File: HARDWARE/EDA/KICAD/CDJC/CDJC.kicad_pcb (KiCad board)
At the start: 2 copper layers, 64 parts, among them J1 COM_IN, J2 COM_OUT, J3 POWER_IN, J4 POWER_OUT, J5 BIT_OUT, Q1 BC549, SW1 B-SET, U1 74LS04, U2 74LS32, U3 74LS08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

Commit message: i am crazy
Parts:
- removed C1: 1800µF 6.3V, Capacitor_THT:CP_Radial_D10.0mm_P5.00mm
- J2, J4, J5: moved to B.Cu
- moved J3 161.1 mm to (182.7, 45.0), turned to 0 degrees
- moved J1 149.6 mm to (182.7, 52.3), turned to 0 degrees
- moved SW1 129.4 mm to (175.0, 51.0), turned to 180 degrees
- moved U1 120.7 mm to (149.5, 81.8), turned to 180 degrees
- moved U4 118.4 mm to (134.0, 135.2), turned to 180 degrees
- moved R6 115.8 mm to (163.4, 53.5)
- moved D3 111.8 mm to (161.1, 45.0), turned to 0 degrees
- moved R3 111.8 mm to (161.2, 53.5)
- moved R5 107.3 mm to (158.2, 53.5)
- moved R2 103.5 mm to (156.0, 53.5)
- moved D2 101.6 mm to (155.9, 45.0), turned to 0 degrees
- moved R4 99.5 mm to (153.1, 53.5)
- moved R1 96.1 mm to (151.0, 53.5)
- moved J4 95.4 mm to (184.2, 117.9)
- moved D1 93.8 mm to (150.7, 45.0), turned to 0 degrees
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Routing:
- net GNDD: track 19.0 -> 87.2 mm
- net LB_SW: track 0.00 -> 20.3 mm
- net +5VD: track 20.0 -> 34.2 mm
- net NB_SW: track 0.00 -> 12.0 mm
- net Net-(U5-Pad10): track 29.2 -> 18.8 mm
- net LBMon: track 10.8 -> 1.04 mm
- net Net-(U8-Pad11): track 0.00 -> 7.62 mm
- net FB_SW: track 0.00 -> 5.01 mm
- net Net-(D1-Pad2): track 0.00 -> 3.50 mm
- net Net-(D2-Pad2): track 0.00 -> 3.48 mm
- net Net-(D3-Pad2): track 0.00 -> 3.48 mm
- net Net-(D5-Pad2): track 0.00 -> 3.45 mm
- net Net-(D7-Pad2): track 0.00 -> 3.43 mm
- net Net-(D8-Pad2): track 0.00 -> 3.42 mm
- net Net-(D6-Pad2): track 0.00 -> 3.40 mm
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
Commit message: i am crazy
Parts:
- D10, D11, D13, D14, D15, D16, D17, D18, D19, D20, D21, D9: footprint Diode_THT:D_DO-34_SOD68_P2.54mm_Vertical_AnodeUp -> Diode_THT:D_DO-34_SOD68_P7.62mm_Horizontal
- J1: footprint Connector_PinHeader_2.00mm:PinHeader_1x05_P2.00mm_Horizontal -> Connector_PinHeader_2.54mm:PinHeader_1x05_P2.54mm_Horizontal
- J2: footprint Connector_PinSocket_2.00mm:PinSocket_1x05_P2.00mm_Horizontal -> Connector_PinSocket_2.54mm:PinSocket_1x05_P2.54mm_Horizontal
- J3: footprint Connector_PinHeader_2.00mm:PinHeader_1x03_P2.00mm_Horizontal -> Connector_PinHeader_2.54mm:PinHeader_1x03_P2.54mm_Horizontal
- J4: footprint Connector_PinSocket_2.00mm:PinSocket_1x03_P2.00mm_Horizontal -> Connector_PinSocket_2.54mm:PinSocket_1x03_P2.54mm_Horizontal
- J5: footprint Connector_PinSocket_2.00mm:PinSocket_1x08_P2.00mm_Horizontal -> Connector_PinSocket_2.54mm:PinSocket_1x08_P2.54mm_Horizontal
- R1, R10, R11, R12, R13, R14, R15, R16, R17, R2, R3, R4, R5, R6, R7, R8, R9: footprint Resistor_THT:R_Axial_DIN0204_L3.6mm_D1.6mm_P5.08mm_Horizontal -> Resistor_THT:R_Axial_DIN0207_L6.3mm_D2.5mm_P7.62mm_Horizontal
- moved SW1 83.1 mm to (92.0, 46.8), turned to 0 degrees
- moved D20 60.9 mm to (95.5, 106.8)
- moved D9 55.8 mm to (100.6, 114.6)
- moved U5 55.8 mm to (113.5, 122.1)
- moved C5 55.8 mm to (105.9, 125.3)
- moved D12 55.8 mm to (118.4, 122.6)
- moved D21 55.8 mm to (103.2, 109.3)
- moved Q1 55.8 mm to (120.2, 112.1)
- moved R15 55.8 mm to (116.2, 106.8)
- moved R16 55.8 mm to (121.2, 117.3)
- moved R17 55.8 mm to (116.2, 117.7)
- moved C8 54.1 mm to (176.8, 95.6), turned to 90 degrees
- moved U4 52.5 mm to (113.2, 87.0), turned to 270 degrees
- moved U7 51.8 mm to (173.6, 88.0), turned to 270 degrees
- moved C3 49.3 mm to (176.8, 76.3), turned to 90 degrees
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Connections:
- U2 pad 1: LB_SW -> GNDD
- U2 pad 10: NB_SW -> LB_SW
- U2 pad 11: Net-(U2-Pad11) -> Net-(U1-Pad9)
- U2 pad 12: GNDD -> FB_SW
- U2 pad 13: GNDD -> NB_SW
- U2 pad 2: NB_SW -> GNDD
- U2 pad 3: Net-(U1-Pad9) -> Net-(U2-Pad3)
- U2 pad 4: FB_SW -> NB_SW
- U2 pad 6: Net-(U1-Pad11) -> Net-(U1-Pad13)
- U2 pad 8: Net-(U1-Pad13) -> Net-(U1-Pad11)
- U3 pad 1: Net-(U1-Pad8) -> Net-(U1-Pad12)
- U3 pad 9: Net-(U1-Pad12) -> Net-(U1-Pad8)
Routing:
- net FB_SW: track 5.01 -> 68.2 mm
- net Net-(U1-Pad13): track 0.00 -> 44.6 mm
- net Net-(U1-Pad11): track 0.00 -> 42.8 mm
- net NB_SW: track 12.0 -> 40.2 mm
- net Net-(U1-Pad9): track 0.00 -> 26.6 mm
- net LB_SW: track 20.3 -> 30.1 mm
- net GNDD: track 87.2 -> 79.6 mm
- net Net-(D5-Pad2): track 3.45 -> 0.00 mm
- net Net-(D7-Pad2): track 3.43 -> 0.00 mm
- net Net-(D8-Pad2): track 3.42 -> 0.00 mm
- net Net-(D6-Pad2): track 3.40 -> 0.00 mm
- net Net-(D4-Pad2): track 3.37 -> 0.00 mm
- net MRI: track 2.50 -> 0.00 mm
- net LBLBI: track 2.50 -> 0.00 mm
- net EI: track 2.50 -> 0.00 mm
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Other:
- board outline added: 116.7 x 101.5 mm

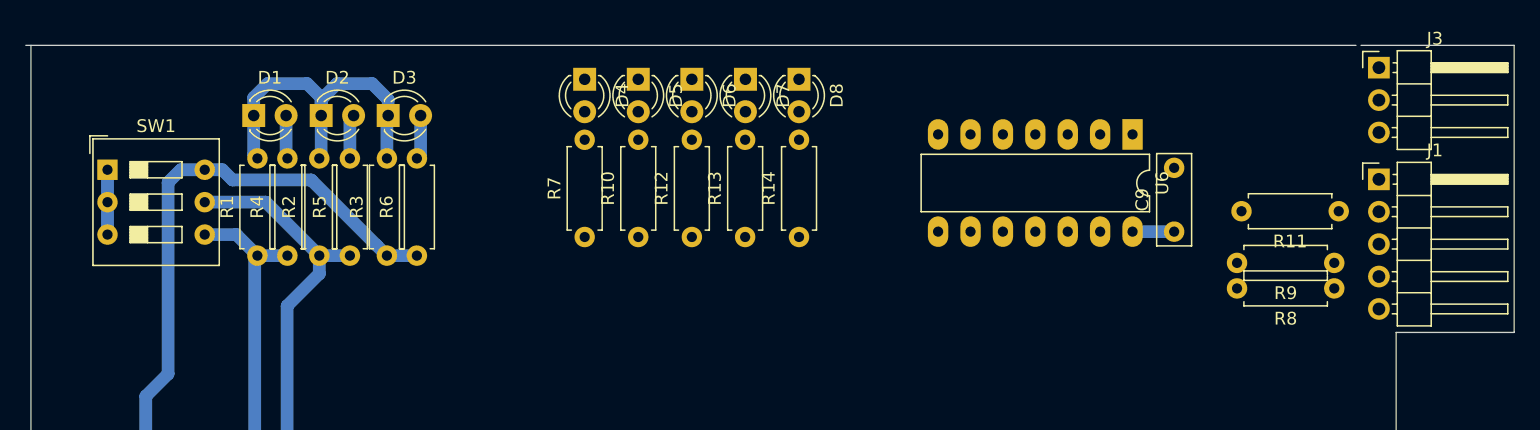
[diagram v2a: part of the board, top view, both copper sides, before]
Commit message: PCI connector OK
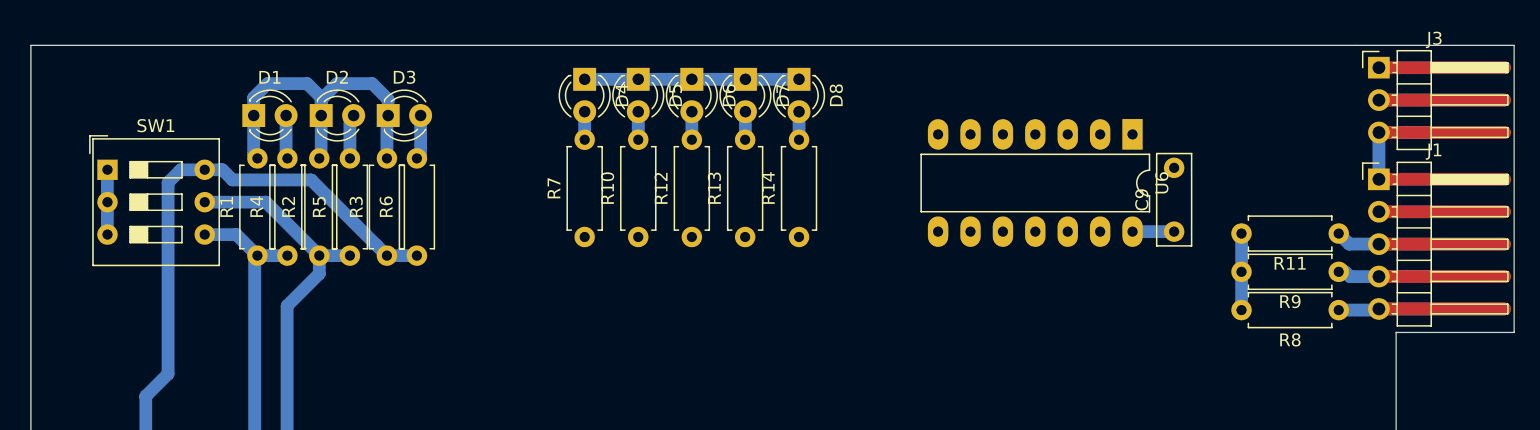
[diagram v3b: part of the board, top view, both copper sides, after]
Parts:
- moved R11 1.75 mm to (188.5, 51.8)
- moved R8 1.74 mm to (188.5, 57.8)
- moved R9 0.78 mm to (188.5, 54.8)
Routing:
- net GNDD: track 79.6 -> 165.2 mm
- net LBLBI: track 0.00 -> 23.2 mm
- net MRI: track 0.00 -> 23.0 mm
- net EI: track 0.00 -> 22.9 mm
- net CLK: track 0.00 -> 19.7 mm
- net +5VD: track 34.7 -> 54.4 mm
- net Net-(D7-Pad2): track 0.00 -> 2.21 mm
- net Net-(D8-Pad2): track 0.00 -> 2.20 mm
- net Net-(D6-Pad2): track 0.00 -> 2.20 mm
- net Net-(D5-Pad2): track 0.00 -> 2.20 mm
- net Net-(D4-Pad2): track 0.00 -> 2.20 mm
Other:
- board size 116.7 x 101.5 mm -> 116.2 x 101.5 mm
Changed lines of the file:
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@@
   (general
     (thickness 1.6)
-    (drawings 7)
-    (tracks 174)
+    (drawings 9)
+    (tracks 206)
     (zones 0)
     (modules 63)
@@
   )
   (module Resistor_THT:R_Axial_DIN0207_L6.3mm_D2.5mm_P7.62mm_Horizontal (layer F.Cu)
-    (at 188.5 50 180)
+    (at 188.5 51.75 180)
     (descr "Resistor, Axial_DIN0207 series, Axial, Horizontal, pin pitch=7.62mm, 0.25W = 1/4W, length*diameter=6.3*2.5mm^2, http://cdn-reichelt.de/documents/datenblatt/B400/1_4W%23YAG.pdf")
     (tags "Resistor Axial_DIN0207 series Axial Horizontal pin pitch 7.62mm 0.25W = 1/4W length 6.3mm diameter 2.5mm")
@@
   )
   (module Resistor_THT:R_Axial_DIN0207_L6.3mm_D2.5mm_P7.62mm_Horizontal (layer F.Cu)
-    (at 188.15 54.05 180)
+    (at 188.5 54.75 180)
     (descr "Resistor, Axial_DIN0207 series, Axial, Horizontal, pin pitch=7.62mm, 0.25W = 1/4W, length*diameter=6.3*2.5mm^2, http://cdn-reichelt.de/documents/datenblatt/B400/1_4W%23YAG.pdf")
     (tags "Resistor Axial_DIN0207 series Axial Horizontal pin pitch 7.62mm 0.25W = 1/4W length 6.3mm diameter 2.5mm")
@@
   )
   (module Resistor_THT:R_Axial_DIN0207_L6.3mm_D2.5mm_P7.62mm_Horizontal (layer F.Cu)
-    (at 188.15 56.05 180)
+    (at 188.5 57.75 180)
     (descr "Resistor, Axial_DIN0207 series, Axial, Horizontal, pin pitch=7.62mm, 0.25W = 1/4W, length*diameter=6.3*2.5mm^2, http://cdn-reichelt.de/documents/datenblatt/B400/1_4W%23YAG.pdf")
     (tags "Resistor Axial_DIN0207 series Axial Horizontal pin pitch 7.62mm 0.25W = 1/4W length 6.3mm diameter 2.5mm")
@@
     )
   )
-  (gr_line (start 85.6 37) (end 189.85 37) (layer Edge.Cuts) (width 0.05))
+  (gr_poly (pts (xy 202.1 59.4) (xy 193 59.4) (xy 193 37.1) (xy 202.1 37.1)) (layer B.Mask) (width 0.1))
+  (gr_poly (pts (xy 202.1 59.4) (xy 193 59.4) (xy 193 37.1) (xy 202.1 37.1)) (layer F.Mask) (width 0.1))
+  (gr_line (start 86 37) (end 189.85 37) (layer Edge.Cuts) (width 0.05))
   (gr_line (start 86 138.5) (end 86 37) (layer Edge.Cuts) (width 0.05))
   (gr_line (start 193 138.5) (end 86 138.5) (layer Edge.Cuts) (width 0.05))
@@
   (gr_line (start 202.25 59.5) (end 193 59.5) (layer Edge.Cuts) (width 0.05))
   (gr_line (start 202.25 37) (end 202.25 59.5) (layer Edge.Cuts) (width 0.05))
-  (gr_line (start 190.25 37) (end 202.25 37) (layer Edge.Cuts) (width 0.05))
+  (gr_line (start 189.85 37) (end 202.25 37) (layer Edge.Cuts) (width 0.05))
+  (segment (start 191.65 50.04) (end 201.5 50.04) (width 1) (layer F.Cu) (net 38))
+  (segment (start 191.65 41.29) (end 201.5 41.29) (width 1) (layer F.Cu) (net 2))
+  (segment (start 191.65 52.58) (end 201.5 52.58) (width 1) (layer F.Cu) (net 37))
+  (segment (start 191.65 57.66) (end 201.5 57.66) (width 1) (layer F.Cu) (net 35))
+  (segment (start 191.65 43.83) (end 201.5 43.83) (width 1) (layer F.Cu) (net 1))
+  (segment (start 191.65 47.5) (end 201.5 47.5) (width 1) (layer F.Cu) (net 1))
+  (segment (start 191.65 38.75) (end 201.5 38.75) (width 1) (layer F.Cu) (net 1))
+  (segment (start 191.65 55.12) (end 201.5 55.12) (width 1) (layer F.Cu) (net 36))
   (segment (start 116.14 106.86) (end 116.15 106.85) (width 1) (layer B.Cu) (net 1))
   (segment (start 113.52 106.86) (end 116.14 106.86) (width 1) (layer B.Cu) (net 1))
@@
   (segment (start 113.7 68.7) (end 115.2 68.7) (width 1) (layer B.Cu) (net 1))
   (segment (start 111.16 68.7) (end 113.7 68.7) (width 1) (layer B.Cu) (net 1))
+  (segment (start 129.4 39.66) (end 146.2 39.66) (width 1) (layer B.Cu) (net 1))
+  (segment (start 180.88 57.75) (end 180.88 51.75) (width 1) (layer B.Cu) (net 1))
+  (segment (start 191.65 43.83) (end 191.65 47.5) (width 1) (layer B.Cu) (net 1))
+  (segment (start 191.65 47.5) (end 201.5 47.5) (width 1) (layer B.Cu) (net 1))
+  (segment (start 191.65 43.83) (end 201.5 43.83) (width 1) (layer B.Cu) (net 1))
+  (segment (start 191.65 38.75) (end 201.5 38.75) (width 1) (layer B.Cu) (net 1))
   (segment (start 116.18 76.32) (end 117 75.5) (width 1) (layer B.Cu) (net 2))
   (segment (start 113.7 76.32) (end 116.18 76.32) (width 1) (layer B.Cu) (net 2))
+  (segment (start 191.65 41.29) (end 201.5 41.29) (width 1) (layer B.Cu) (net 2))
+  (segment (start 129.4 42.2) (end 129.4 44.4) (width 1) (layer B.Cu) (net 6))
+  (segment (start 133.6 42.2) (end 133.6 44.4) (width 1) (layer B.Cu) (net 7))
+  (segment (start 137.8 42.2) (end 137.8 44.4) (width 1) (layer B.Cu) (net 8))
+  (segment (start 142 44.376969) (end 141.976969 44.4) (width 1) (layer B.Cu) (net 9))
+  (segment (start 142 42.2) (end 142 44.376969) (width 1) (layer B.Cu) (net 9))
+  (segment (start 146.2 42.2) (end 146.2 44.4) (width 1) (layer B.Cu) (net 10))
+  (segment (start 191.56 57.75) (end 191.65 57.66) (width 1) (layer B.Cu) (net 35))
+  (segment (start 188.5 57.75) (end 191.56 57.75) (width 1) (layer B.Cu) (net 35))
+  (segment (start 191.65 57.66) (end 201.5 57.66) (width 1) (layer B.Cu) (net 35))
+  (segment (start 188.5 54.75) (end 189 54.75) (width 1) (layer B.Cu) (net 36))
+  (segment (start 189.37 55.12) (end 191.65 55.12) (width 1) (layer B.Cu) (net 36))
+  (segment (start 189 54.75) (end 189.37 55.12) (width 1) (layer B.Cu) (net 36))
+  (segment (start 191.65 55.12) (end 201.5 55.12) (width 1) (layer B.Cu) (net 36))
+  (segment (start 189.33 52.58) (end 191.65 52.58) (width 1) (layer B.Cu) (net 37))
+  (segment (start 188.5 51.75) (end 189.33 52.58) (width 1) (layer B.Cu) (net 37))
+  (segment (start 191.65 52.58) (end 201.5 52.58) (width 1) (layer B.Cu) (net 37))
+  (segment (start 191.65 50.04) (end 201.5 50.04) (width 1) (layer B.Cu) (net 38))
   (segment (start 111.16 74.12) (end 109.04 72) (width 1) (layer B.Cu) (net 42))
   (segment (start 111.16 76.32) (end 111.16 74.12) (width 1) (layer B.Cu) (net 42))

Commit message: stop work
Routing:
- net LBLBI: track 23.2 -> 87.5 mm
- net MRI: track 23.0 -> 62.2 mm
- net FBMon: track 0.00 -> 37.5 mm
- net MRLMon: track 0.00 -> 29.2 mm, vias 0 -> 1
- net EI: track 22.9 -> 50.0 mm
- net Net-(U6-Pad11): track 0.00 -> 17.7 mm
- net LBMon: track 1.04 -> 17.3 mm
- net Net-(U6-Pad2): track 0.00 -> 9.46 mm
- net LB_SW: track 30.1 -> 34.4 mm, vias 0 -> 1
- net GNDD: track 165.2 -> 168.5 mm
- net Net-(U1-Pad11): track 42.8 -> 44.2 mm
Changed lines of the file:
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@@
     (thickness 1.6)
     (drawings 9)
-    (tracks 206)
+    (tracks 261)
     (zones 0)
     (modules 63)
@@
   (segment (start 191.65 43.83) (end 201.5 43.83) (width 1) (layer B.Cu) (net 1))
   (segment (start 191.65 38.75) (end 201.5 38.75) (width 1) (layer B.Cu) (net 1))
+  (segment (start 96.66 68.7) (end 95.6 69.76) (width 1) (layer F.Cu) (net 1))
+  (segment (start 98.46 68.7) (end 96.66 68.7) (width 1) (layer F.Cu) (net 1))
   (segment (start 116.18 76.32) (end 117 75.5) (width 1) (layer B.Cu) (net 2))
   (segment (start 113.7 76.32) (end 116.18 76.32) (width 1) (layer B.Cu) (net 2))
@@
   (segment (start 188.5 57.75) (end 191.56 57.75) (width 1) (layer B.Cu) (net 35))
   (segment (start 191.65 57.66) (end 201.5 57.66) (width 1) (layer B.Cu) (net 35))
+  (segment (start 179.18 43.98) (end 172.34 43.98) (width 1) (layer B.Cu) (net 35))
+  (segment (start 182.6 47.4) (end 179.18 43.98) (width 1) (layer B.Cu) (net 35))
+  (segment (start 182.6 56.4) (end 182.6 47.4) (width 1) (layer B.Cu) (net 35))
+  (segment (start 183.95 57.75) (end 182.6 56.4) (width 1) (layer B.Cu) (net 35))
+  (segment (start 188.5 57.75) (end 183.95 57.75) (width 1) (layer B.Cu) (net 35))
   (segment (start 188.5 54.75) (end 189 54.75) (width 1) (layer B.Cu) (net 36))
   (segment (start 189.37 55.12) (end 191.65 55.12) (width 1) (layer B.Cu) (net 36))
   (segment (start 189 54.75) (end 189.37 55.12) (width 1) (layer B.Cu) (net 36))
   (segment (start 191.65 55.12) (end 201.5 55.12) (width 1) (layer B.Cu) (net 36))
+  (segment (start 188.5 54.75) (end 185.35 54.75) (width 1) (layer B.Cu) (net 36))
+  (segment (start 185.35 54.75) (end 184.3 53.7) (width 1) (layer B.Cu) (net 36))
+  (segment (start 184.3 53.7) (end 184.3 45.4) (width 1) (layer B.Cu) (net 36))
+  (segment (start 184.3 45.4) (end 180.1 41.2) (width 1) (layer B.Cu) (net 36))
+  (segment (start 162.18 41.78) (end 162.18 43.98) (width 1) (layer B.Cu) (net 36))
+  (segment (start 162.76 41.2) (end 162.18 41.78) (width 1) (layer B.Cu) (net 36))
+  (segment (start 180.1 41.2) (end 162.76 41.2) (width 1) (layer B.Cu) (net 36))
   (segment (start 189.33 52.58) (end 191.65 52.58) (width 1) (layer B.Cu) (net 37))
   (segment (start 188.5 51.75) (end 189.33 52.58) (width 1) (layer B.Cu) (net 37))
   (segment (start 191.65 52.58) (end 201.5 52.58) (width 1) (layer B.Cu) (net 37))
+  (segment (start 159.64 53.8) (end 159.64 51.6) (width 1) (layer B.Cu) (net 37))
+  (segment (start 159.04 54.4) (end 159.64 53.8) (width 1) (layer B.Cu) (net 37))
+  (segment (start 153.8 51.6) (end 156.6 54.4) (width 1) (layer B.Cu) (net 37))
+  (segment (start 181.3 39.1) (end 156.3 39.1) (width 1) (layer B.Cu) (net 37))
+  (segment (start 153.8 41.6) (end 153.8 51.6) (width 1) (layer B.Cu) (net 37))
+  (segment (start 156.3 39.1) (end 153.8 41.6) (width 1) (layer B.Cu) (net 37))
+  (segment (start 186.4 44.2) (end 181.3 39.1) (width 1) (layer B.Cu) (net 37))
+  (segment (start 156.6 54.4) (end 159.04 54.4) (width 1) (layer B.Cu) (net 37))
+  (segment (start 186.4 50.78137) (end 186.4 44.2) (width 1) (layer B.Cu) (net 37))
+  (segment (start 187.36863 51.75) (end 186.4 50.78137) (width 1) (layer B.Cu) (net 37))
+  (segment (start 188.5 51.75) (end 187.36863 51.75) (width 1) (layer B.Cu) (net 37))
   (segment (start 191.65 50.04) (end 201.5 50.04) (width 1) (layer B.Cu) (net 38))
+  (segment (start 103.54 78.53999) (end 105 79.99999) (width 1) (layer B.Cu) (net 41))
+  (segment (start 103.54 76.32) (end 103.54 78.53999) (width 1) (layer B.Cu) (net 41))
+  (via (at 105 79.99999) (size 0.8) (drill 0.4) (layers F.Cu B.Cu) (net 41))
   (segment (start 111.16 74.12) (end 109.04 72) (width 1) (layer B.Cu) (net 42))
   (segment (start 111.16 76.32) (end 111.16 74.12) (width 1) (layer B.Cu) (net 42))
@@
   (segment (start 108.39 78.75) (end 108.62 78.52) (width 1) (layer F.Cu) (net 43))
   (segment (start 101.23 78.75) (end 108.39 78.75) (width 1) (layer F.Cu) (net 43))
+  (segment (start 130.199999 52.819999) (end 129.4 52.02) (width 1) (layer B.Cu) (net 44))
+  (segment (start 132.98001 55.60001) (end 130.199999 52.819999) (width 1) (layer B.Cu) (net 44))
+  (segment (start 160.79999 55.60001) (end 132.98001 55.60001) (width 1) (layer B.Cu) (net 44))
+  (segment (start 162.18 54.22) (end 160.79999 55.60001) (width 1) (layer B.Cu) (net 44))
+  (segment (start 162.18 51.6) (end 162.18 54.22) (width 1) (layer B.Cu) (net 44))
   (segment (start 171.06 87.98) (end 171.06 88.56) (width 1) (layer B.Cu) (net 46))
   (segment (start 171.06 87.98) (end 171.06 87.58) (width 1) (layer B.Cu) (net 46))
   (segment (start 171.06 87.58) (end 171.1 87.54) (width 1) (layer B.Cu) (net 46))
+  (segment (start 171.06 85.78) (end 167.58 82.3) (width 1) (layer B.Cu) (net 46))
+  (segment (start 171.06 87.98) (end 171.06 85.78) (width 1) (layer B.Cu) (net 46))
+  (segment (start 167.58 82.3) (end 165 82.3) (width 1) (layer B.Cu) (net 46))
+  (segment (start 163.44 80.74) (end 163.44 76.35) (width 1) (layer B.Cu) (net 46))
+  (segment (start 165 82.3) (end 163.44 80.74) (width 1) (layer B.Cu) (net 46))
+  (via (at 147.8 57.4) (size 0.8) (drill 0.4) (layers F.Cu B.Cu) (net 48))
+  (segment (start 167.26 51.6) (end 167.26 53.8) (width 1) (layer B.Cu) (net 48))
+  (segment (start 167.26 53.8) (end 163.66 57.4) (width 1) (layer B.Cu) (net 48))
+  (segment (start 163.66 57.4) (end 148.365685 57.4) (width 1) (layer B.Cu) (net 48))
+  (segment (start 148.365685 57.4) (end 147.8 57.4) (width 1) (layer B.Cu) (net 48))
+  (segment (start 146.2 55.8) (end 147.8 57.4) (width 1) (layer F.Cu) (net 48))
+  (segment (start 146.2 52.02) (end 146.2 55.8) (width 1) (layer F.Cu) (net 48))
   (segment (start 140.8 73.55) (end 140.8 76.12) (width 1) (layer F.Cu) (net 49))
   (segment (start 139.5 72.25) (end 140.8 73.55) (width 1) (layer F.Cu) (net 49))
@@
   (segment (start 101 69.1) (end 104.15 72.25) (width 1) (layer F.Cu) (net 49))
   (segment (start 101 68.7) (end 101 69.1) (width 1) (layer F.Cu) (net 49))
-  (segment (start 98.46 78.52) (end 99.44 79.5) (width 1) (layer B.Cu) (net 52))
-  (segment (start 98.46 76.32) (end 98.46 78.52) (width 1) (layer B.Cu) (net 52))
-  (segment (start 99.44 79.5) (end 135 79.5) (width 1) (layer B.Cu) (net 52))
+  (segment (start 133.3 81.2) (end 135.72 78.78) (width 1) (layer B.Cu) (net 52))
+  (segment (start 101.14 81.2) (end 133.3 81.2) (width 1) (layer B.Cu) (net 52))
   (segment (start 135.72 78.78) (end 135.72 76.12) (width 1) (layer B.Cu) (net 52))
-  (segment (start 135 79.5) (end 135.72 78.78) (width 1) (layer B.Cu) (net 52))
+  (segment (start 98.46 78.52) (end 101.14 81.2) (width 1) (layer B.Cu) (net 52))
+  (segment (start 98.46 76.32) (end 98.46 78.52) (width 1) (layer B.Cu) (net 52))
   (segment (start 128.27 73.75) (end 130.64 76.12) (width 1) (layer F.Cu) (net 55))
   (segment (start 108.65 73.75) (end 128.27 73.75) (width 1) (layer F.Cu) (net 55))
@@
   (segment (start 158.36 95.6) (end 158.36 93.4) (width 1) (layer B.Cu) (net 69))
   (segment (start 158.36 93.4) (end 159.91 91.85) (width 1) (layer B.Cu) (net 69))
+  (segment (start 164.72 51.6) (end 164.72 62.08) (width 1) (layer F.Cu) (net 71))
+  (segment (start 163.44 63.36) (end 163.44 68.73) (width 1) (layer F.Cu) (net 71))
+  (segment (start 164.72 62.08) (end 163.44 63.36) (width 1) (layer F.Cu) (net 71))
+  (segment (start 164.72 42.08) (end 164.72 43.98) (width 1) (layer F.Cu) (net 72))
+  (segment (start 165.5 41.3) (end 164.72 42.08) (width 1) (layer F.Cu) (net 72))
+  (segment (start 168.9 41.3) (end 165.5 41.3) (width 1) (layer F.Cu) (net 72))
+  (segment (start 169.7 42.1) (end 168.9 41.3) (width 1) (layer F.Cu) (net 72))
+  (segment (start 169.7 43.48) (end 169.7 42.1) (width 1) (layer F.Cu) (net 72))
+  (segment (start 169.8 43.58) (end 169.7 43.48) (width 1) (layer F.Cu) (net 72))
+  (segment (start 169.8 43.98) (end 169.8 43.58) (width 1) (layer F.Cu) (net 72))
 )
